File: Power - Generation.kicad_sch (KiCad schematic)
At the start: 0 parts

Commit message: added tps61252 boost converter and started working on power - generatio and on/off control schematic
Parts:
- added C44: 100nF, 0_capacitors:C_0402_1005Metric, symbol 0_capacitors:CL05B104KO5NNNC
- added D2, D3: 1N5819WS, 0_diodes:D_SOD-323, symbol 0_diodes:1N5819WS
- added Q1, Q2: AO3400A, Package_TO_SOT_SMD:SOT-23, symbol 0_transistors:AO3400A
- added R53, R55, R56, R60: 47kΩ, 0_resistors:R_0402_1005Metric, symbol 0_resistors:0402WGF4702TCE
- added R57, R58: 10kΩ, 0_resistors:R_0402_1005Metric, symbol 0_resistors:0402WGF1002TCE
- added R59: 5.1kΩ, 0_resistors:R_0402_1005Metric, symbol 0_resistors:0402WGF5101TCE
- added SI2301CDS-T1-GE1: Q_PMOS_GSD, 0_transistors:SOT-23, symbol 0_transistors:Q_PMOS_GSD
- added SW8: Button SPST SMD Tactile Switch, 0_switches:SW_TS-1088-AR02016, symbol 0_switches:SW_Push
- added U5: TPS61252DSG, Package_SON:WSON-8-1EP_2x2mm_P0.5mm_EP0.9x1.6mm, symbol 0_integrated_circuits:TPS61252DSG
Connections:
- new net: U5.1 (GND), U5.9 (GND)
- new net: C44.1, R59.2, R60.2
- new net +3.3V: R60.1
- new net GND: C44.2, SW8.2
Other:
- note added: "http://www.mosaic-industries.com/embedded-systems/microcontroller-projects/electronic-circuits/push-button-switch-turn-on/microcontroller-latching-on-off"

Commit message: added power switch, 5V and 3V3 power generation
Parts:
- removed C44: 100nF, 0_capacitors:C_0402_1005Metric, symbol 0_capacitors:CL05B104KO5NNNC
- removed D2: 1N5819WS, 0_diodes:D_SOD-323, symbol 0_diodes:1N5819WS
- removed R53, R55, R60: 47kΩ, 0_resistors:R_0402_1005Metric, symbol 0_resistors:0402WGF4702TCE
- removed R58: 10kΩ, 0_resistors:R_0402_1005Metric, symbol 0_resistors:0402WGF1002TCE
- removed R59: 5.1kΩ, 0_resistors:R_0402_1005Metric, symbol 0_resistors:0402WGF5101TCE
- removed SI2301CDS-T1-GE1: Q_PMOS_GSD, 0_transistors:SOT-23, symbol 0_transistors:Q_PMOS_GSD
- added C44, C45: 10uF, 0_capacitors:C_0805_2012Metric, symbol 0_capacitors:CL21A106KAYNNNE
- added C46: 1uF, 0_capacitors:C_0603_1608Metric, symbol 0_capacitors:CL10A105KB8NNNC
- added C47, C53, C54: 100nF, 0_capacitors:C_0402_1005Metric, symbol 0_capacitors:CL05B104KO5NNNC
- added C48: 100pF, 0_capacitors:C_0603_1608Metric, symbol 0_capacitors:CL10C101JB8NNNC
- added C49, C50: 22uF, 0_capacitors:C_0805_2012Metric, symbol 0_capacitors:CL21A226MAQNNNE
- added C51, C52: 10uF 16V, 0_capacitors:CP_EIA-3216-18_Kemet-A, symbol 0_capacitors:TAJA106K016RNJ
- added L4: 1.8A 1uH, Inductor_SMD:L_Cenker_CKCS4018, symbol 0_inductors:CKCS4018-1.5uH/N
- added Q3: SI2301CDS-T1-GE3, 0_transistors:SOT-23, symbol 0_transistors:Q_PMOS_GSD
- added R53, R60, R62, R66: 100kΩ, 0_resistors:R_0402_1005Metric, symbol 0_resistors:0402WGF1003TCE
- added R54, R55, R58, R59, R61: 0Ω, 0_resistors:R_0402_1005Metric, symbol 0_resistors:0402WGF0000TCE
- added R63: 330Ω, 0_resistors:R_0402_1005Metric, symbol 0_resistors:0402WGF3300TCE
- added R64: 300kΩ, 0_resistors:R_0603_1608Metric, symbol 0_resistors:0603WAF3003T5E
- added R65: 1kΩ, 0_resistors:R_0402_1005Metric, symbol 0_resistors:0402WGF1001TCE
- added R67: 634kΩ, 0_resistors:R_0402_1005Metric, symbol 0_resistors:RC-02W6343FT
- added U4: AMS1117-3.3, Package_TO_SOT_SMD:SOT-223-3_TabPin2, symbol Regulator_Linear:AMS1117-3.3
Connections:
- net +3.3V: now also C52.1, C54.1, U4.2 (VO)
- net GND: now also Q1.2 (S), Q2.2 (S), R56.2, U5.1 (GND), C44.2, C49.2, C50.2, C51.2, C52.2, C53.2, C54.2, R55.2, R66.2, U4.1 (GND)
- net VBUS: now also R63.1
- net VSYS: now also R57.2, C47.1, Q3.2 (S), R53.1, R61.1
- net uC_PWR: now also R65.2
- net at U5.9 (GND): no longer U5.1 (GND)
- net +5V: now reaches U5.2 (VOUT)
- net +5V: now also C48.1, C49.1, C50.1, C51.1, C53.1, R67.1, U4.3 (VI)
- net at U5.3 (FB): now also C48.2, R60.1, R67.2
- net at U5.4 (ILIM): now also R55.1, R59.2
- net VSYS_SW: now reaches U5.6 (EN)
- net VSYS_SW: now also U5.8 (VIN), C44.1, C45.1, L4.1, Q3.3 (D), R59.1, R61.2, R62.1
- net at U5.7 (SW): now also L4.2
- net at R56.1: now also Q2.1 (G), R63.2
- net at SW8.1: now also D3.1 (K), R57.1, C46.1
- net uC_CTRL: now reaches D3.2 (A)
- net uC_CTRL: now also R62.2, R64.1, R65.1
- net VBUS_CTRL: now reaches Q2.3 (D)
- net VBUS_CTRL: now also R58.2
- net at Q1.1 (G): now also C45.2, R64.2
- net at Q1.3 (D): now also R54.2
- new net: C46.2, C47.2, Q3.1 (G), R53.2, R54.1, R58.1
- new net: R60.2, R66.1
- no-connect marks 0 -> 1
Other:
- note removed: "http://www.mosaic-industries.com/embedded-systems/microcontroller-projects/electronic-circuits/push-button-switch-turn-on/microcontroller-latching-on-off"
- title: (none) -> Power - Generation and Switch
- moved on the sheet: D3, Q1, Q2, R56, R57, SW8, U5

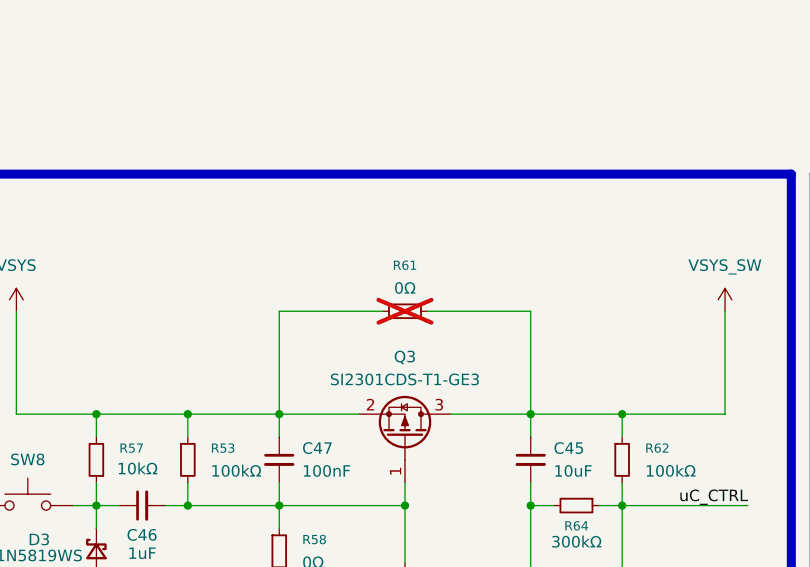
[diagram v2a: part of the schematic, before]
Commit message: added power for mcu
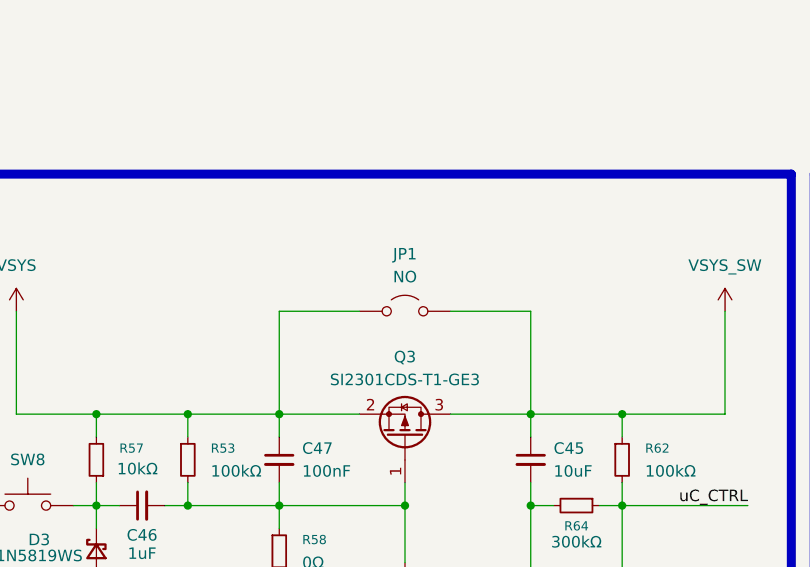
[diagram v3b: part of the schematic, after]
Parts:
- removed R61: 0Ω, 0_resistors:R_0402_1005Metric, symbol 0_resistors:0402WGF0000TCE
- added JP1: NO, Jumper:SolderJumper-2_P1.3mm_Open_TrianglePad1.0x1.5mm, symbol 0_modules:Jumper_2_Open
- U4: Supplier 1 (none) -> JLCPCB; Supplier Part Number 1 (none) -> C6186
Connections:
- net VSYS: now also JP1.1 (A)
- net VSYS_SW: now also JP1.2 (B)
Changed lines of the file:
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@@
 	(wire
 		(pts
-			(xy 130.81 87.63) (xy 142.24 87.63)
+			(xy 130.81 87.63) (xy 139.7 87.63)
 		)
 		(stroke
@@
 	(wire
 		(pts
-			(xy 158.75 87.63) (xy 147.32 87.63)
+			(xy 158.75 87.63) (xy 149.86 87.63)
 		)
 		(stroke
@@
 				(path "/0650c7a8-acba-429c-9f8e-eec0baf0bc1c/fede4c36-00cc-4d3d-b71c-5243ba232202/d9b656b6-4698-4330-a229-95286576934d"
 					(reference "C51")
+					(unit 1)
+				)
+			)
+		)
+	)
+	(symbol
+		(lib_id "0_modules:Jumper_2_Open")
+		(at 144.78 87.63 0)
+		(unit 1)
+		(exclude_from_sim no)
+		(in_bom yes)
+		(on_board yes)
+		(dnp no)
+		(fields_autoplaced yes)
+		(property "Reference" "JP1"
+			(at 144.78 81.28 0)
+			(effects
+				(font
+					(size 1.27 1.27)
+				)
+			)
+		)
+		(property "Value" "NO"
+			(at 144.78 83.82 0)
+			(effects
+				(font
+					(size 1.27 1.27)
+				)
+			)
+		)
+		(property "Footprint" "Jumper:SolderJumper-2_P1.3mm_Open_TrianglePad1.0x1.5mm"
+			(at 144.78 87.63 0)
+			(effects
+				(font
+					(size 1.27 1.27)
+				)
+				(hide yes)
+			)
+		)
+		(property "Datasheet" "~"
+			(at 144.78 87.63 0)
+			(effects
+				(font
+					(size 1.27 1.27)
+				)
+				(hide yes)
+			)
+		)
+		(property "Description" "Jumper, 2-pole, open"
+			(at 144.78 87.63 0)
+			(effects
+				(font
+					(size 1.27 1.27)
+				)
+				(hide yes)
+			)
+		)
+		(pin "2"
+		)
+		(pin "1"
+		)
+		(instances
+			(project ""
+				(path "/0650c7a8-acba-429c-9f8e-eec0baf0bc1c/fede4c36-00cc-4d3d-b71c-5243ba232202/d9b656b6-4698-4330-a229-95286576934d"
+					(reference "JP1")
 					(unit 1)
 				)
@@
 	)
 	(symbol
-		(lib_id "0_resistors:0402WGF0000TCE")
-		(at 144.78 87.63 90)
-		(unit 1)
-		(exclude_from_sim no)
-		(in_bom no)
-		(on_board yes)
-		(dnp yes)
-		(fields_autoplaced yes)
-		(property "Reference" "R61"
-			(at 144.78 82.55 90)
-			(effects
-				(font
-					(size 1.016 1.016)
-				)
-			)
-		)
-		(property "Value" "0Ω"
-			(at 144.78 85.09 90)
-			(effects
-				(font
-					(size 1.27 1.27)
-				)
-			)
-		)
-		(property "Footprint" "0_resistors:R_0402_1005Metric"
-			(at 144.78 87.63 0)
-			(effects
-				(font
-					(size 1.27 1.27)
-				)
-				(hide yes)
-			)
-		)
-		(property "Datasheet" "~"
-			(at 144.78 87.63 0)
-			(effects
-				(font
-					(size 1.27 1.27)
-				)
-				(hide yes)
-			)
-		)
-		(property "Description" "50V ±800ppm/℃ ±1% 0Ω 0402"
-			(at 144.78 87.63 0)
-			(effects
-				(font
-					(size 1.27 1.27)
-				)
-				(hide yes)
-			)
-		)
-		(property "Supplier 1" "JLCPCB"
-			(at 144.78 87.63 0)
-			(effects
-				(font
-					(size 1.27 1.27)
-				)
-				(hide yes)
-			)
-		)
-		(property "Supplier Part Number 1" "C17168"
-			(at 144.78 87.63 0)
-			(effects
-				(font
-					(size 1.27 1.27)
-				)
-				(hide yes)
-			)
-		)
-		(pin "1"
-		)
-		(pin "2"
-		)
-		(instances
-			(project ""
-				(path "/0650c7a8-acba-429c-9f8e-eec0baf0bc1c/fede4c36-00cc-4d3d-b71c-5243ba232202/d9b656b6-4698-4330-a229-95286576934d"
-					(reference "R61")
-					(unit 1)
-				)
-			)
-		)
-	)
-	(symbol
 		(lib_id "0_resistors:0402WGF3300TCE")
 		(at 113.03 168.91 90)
@@
 			(at 250.19 168.91 0)
 			(effects
+				(font
+					(size 1.27 1.27)
+				)
+				(hide yes)
+			)
+		)
+		(property "Supplier 1" "JLCPCB"
+			(at 250.19 168.91 0)
+			(effects
+				(font
+					(size 1.27 1.27)
+				)
+				(hide yes)
+			)
+		)
+		(property "Supplier Part Number 1" "C6186"
+			(at 250.19 168.91 0)
+			(effects

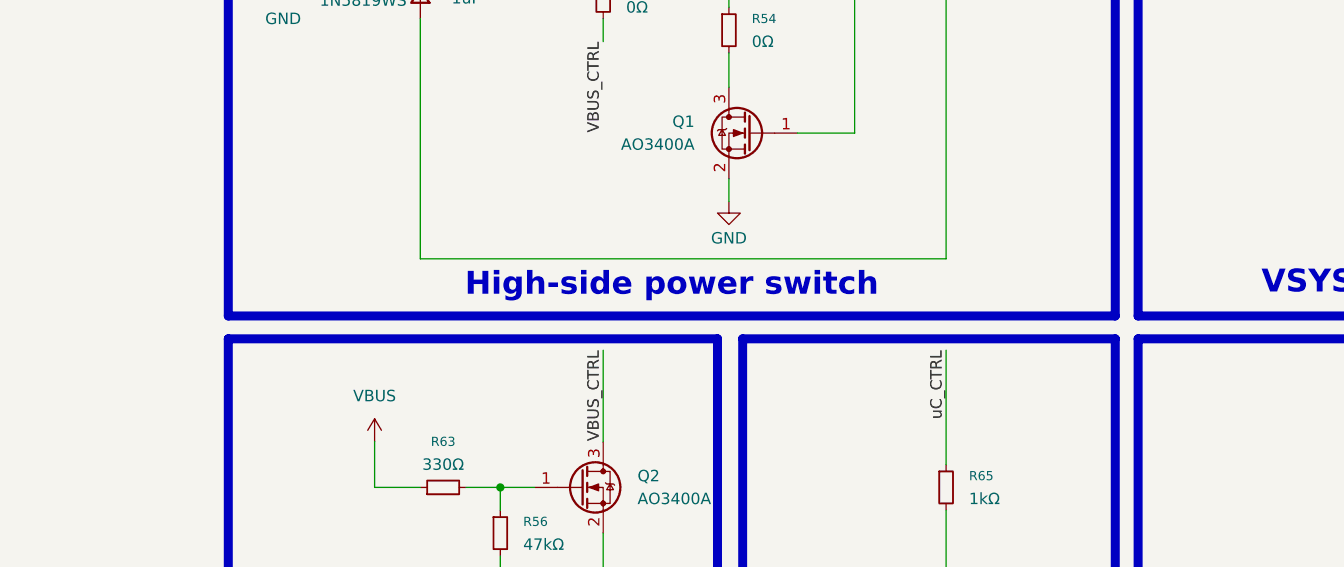
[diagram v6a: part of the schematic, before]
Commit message: added auxiliary schematic, problem with kicad - cannot modify project settings
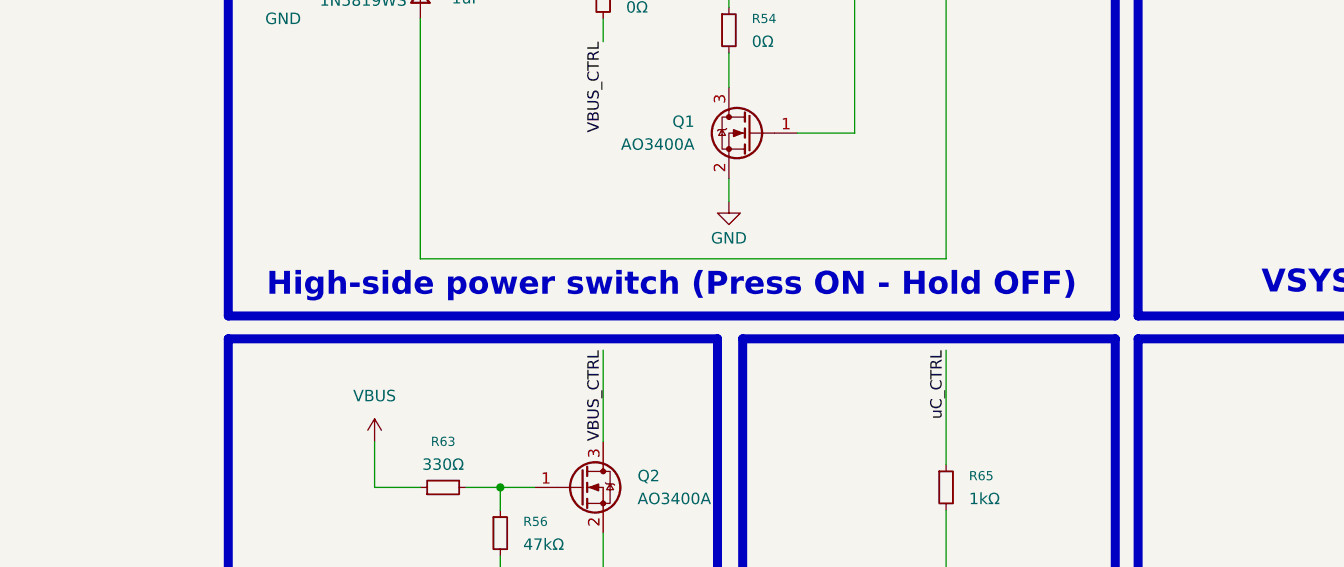
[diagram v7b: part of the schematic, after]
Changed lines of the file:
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@@
 		)
 	)
-	(text_box "High-side power switch"
+	(text_box "High-side power switch (Press ON - Hold OFF)"
 		(exclude_from_sim no)
 		(at 89.662 136.906 0)
@@
 		(polyline
 			(pts
-				(xy 287.02 102.87) (xy 307.34 102.87) (xy 307.34 90.17) (xy 287.02 90.17)
+				(xy 214.884 100.33) (xy 214.884 107.696) (xy 229.87 107.696) (xy 229.87 100.33) (xy 246.38 100.33)
+				(xy 246.38 85.09) (xy 214.884 85.09)
 			)
 			(stroke
@@
 		(polyline
 			(pts
-				(xy 214.884 100.33) (xy 214.884 107.696) (xy 229.87 107.696) (xy 229.87 100.33) (xy 246.38 100.33)
-				(xy 246.38 85.09) (xy 214.884 85.09)
+				(xy 287.02 102.87) (xy 307.34 102.87) (xy 307.34 90.17) (xy 287.02 90.17)
 			)
 			(stroke
